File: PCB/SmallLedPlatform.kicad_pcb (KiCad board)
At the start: 4 copper layers, 63.5 x 36.1 mm, 121 parts, among them J101 Conn_01x03_Male, J102 USB_C_Receptacle, J103 Conn_01x03_Male, J104 Conn_02x05_Odd_Even, M101 Fan_4pin, Q101 AO3400A, Q201 IRFR7440TRPBF, Q202 IRFR7440TRPBF, Q301 2N7002, Q302 2N7002, Q303 2N7002, Q304 2N7002, SW401 SW_MEC_5E, SW402 SW_MEC_5E, U101 STM32G0B1CBTx, U102 USBLC6-2P6, U103 TCPP01-M12, U201 LM25118, U202 XC6206PxxxMR, U203 WS3222D, U204 WS3222D, U401 AP3722AT

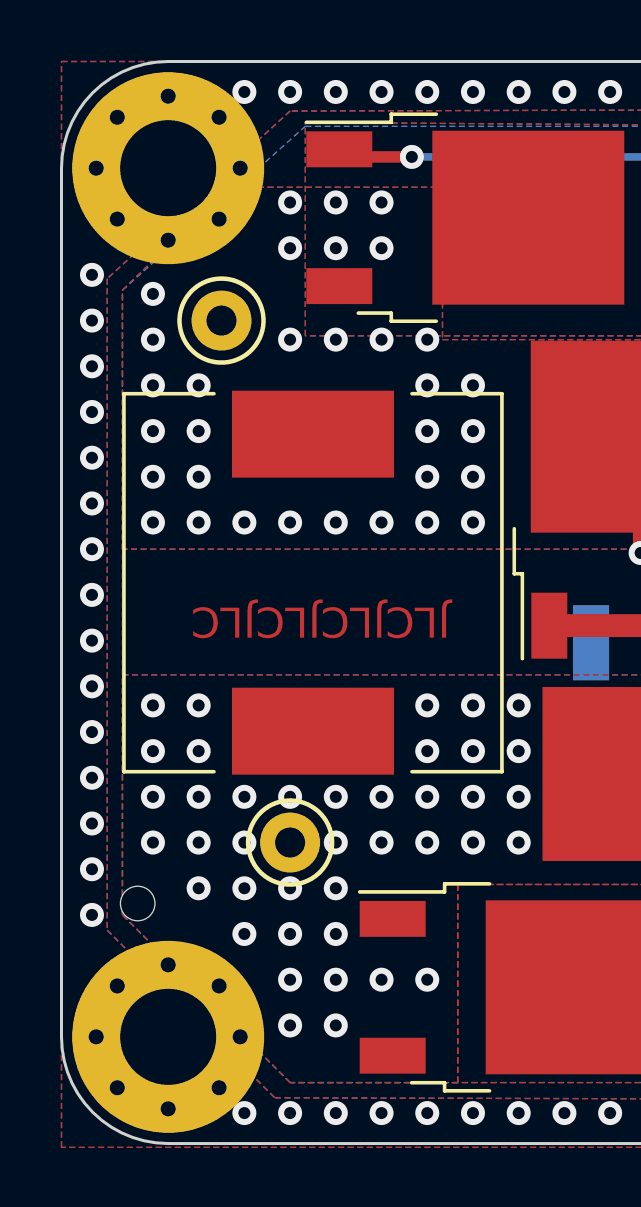
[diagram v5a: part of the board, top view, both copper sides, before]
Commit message: Added hole for fan cable entry
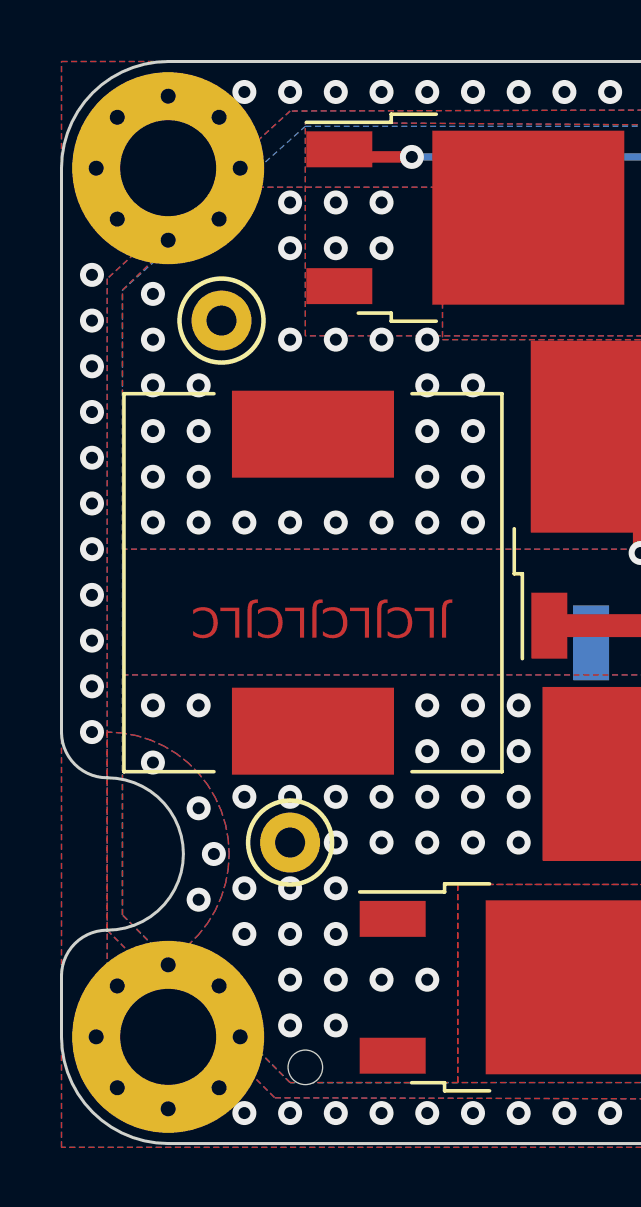
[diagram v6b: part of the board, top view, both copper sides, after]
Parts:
- moved H105 7.81 mm to (99.6, 112.3)
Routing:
- net /Power/dcdc_coil: vias 40 -> 32
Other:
- outline, holes or cut-outs redrawn
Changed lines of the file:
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@@
   )
   (footprint "JLC:JLC_toolinghole" (layer "F.Cu")
-    (at 93.98 106.807)
+    (at 99.568 112.268)
     (property "Sheetfile" "SmallLedPlatform.kicad_sch")
     (property "Sheetname" "")
@@
   (gr_line (start 94.996 78.74) (end 151.384 78.74) (layer "Edge.Cuts") (width 0.1))
   (gr_line (start 154.94 82.296) (end 154.94 111.252) (layer "Edge.Cuts") (width 0.1))
-  (gr_line (start 91.44 111.252) (end 91.44 82.296) (layer "Edge.Cuts") (width 0.1))
+  (gr_line (start 91.44 111.252) (end 91.44 109.22) (layer "Edge.Cuts") (width 0.1))
   (gr_arc (start 151.384 78.74) (mid 153.898472 79.781528) (end 154.94 82.296) (layer "Edge.Cuts") (width 0.1))
   (gr_arc (start 91.44 82.296) (mid 92.481528 79.781528) (end 94.996 78.74) (layer "Edge.Cuts") (width 0.1))
+  (gr_arc (start 91.44 109.22) (mid 91.886369 108.142369) (end 92.964 107.696) (layer "Edge.Cuts") (width 0.1))
+  (gr_arc (start 92.964 102.616) (mid 95.504 105.156) (end 92.964 107.696) (layer "Edge.Cuts") (width 0.1))
+  (gr_arc (start 92.964 102.616) (mid 91.886369 102.169631) (end 91.44 101.092) (layer "Edge.Cuts") (width 0.1))
+  (gr_line (start 91.44 101.092) (end 91.44 82.296) (layer "Edge.Cuts") (width 0.1))
   (gr_arc (start 94.996 114.808) (mid 92.481528 113.766472) (end 91.44 111.252) (layer "Edge.Cuts") (width 0.1))
   (gr_text "JLCJLCJLCJLC" (at 100.076 97.409 180) (layer "F.Cu")
@@
   (via (at 108.204 79.756) (size 0.8) (drill 0.4) (layers "F.Cu" "B.Cu") (free) (net 7))
   (via (at 99.06 79.756) (size 0.8) (drill 0.4) (layers "F.Cu" "B.Cu") (free) (net 7))
+  (via (at 96.012 106.68) (size 0.8) (drill 0.4) (layers "F.Cu" "B.Cu") (free) (net 7))
   (via (at 129.54 113.792) (size 0.8) (drill 0.4) (layers "F.Cu" "B.Cu") (free) (net 7))
   (via (at 126.492 79.756) (size 0.8) (drill 0.4) (layers "F.Cu" "B.Cu") (free) (net 7))
@@
   (via (at 92.456 101.092) (size 0.8) (drill 0.4) (layers "F.Cu" "B.Cu") (free) (net 7))
   (via (at 92.456 93.472) (size 0.8) (drill 0.4) (layers "F.Cu" "B.Cu") (free) (net 7))
+  (via (at 94.488 102.108) (size 0.8) (drill 0.4) (layers "F.Cu" "B.Cu") (free) (net 7))
   (via (at 103.632 113.792) (size 0.8) (drill 0.4) (layers "F.Cu" "B.Cu") (free) (net 7))
   (via (at 105.156 113.792) (size 0.8) (drill 0.4) (layers "F.Cu" "B.Cu") (free) (net 7))
@@
   (via (at 92.456 99.568) (size 0.8) (drill 0.4) (layers "F.Cu" "B.Cu") (free) (net 7))
   (via (at 140.208 113.792) (size 0.8) (drill 0.4) (layers "F.Cu" "B.Cu") (free) (net 7))
-  (via (at 92.456 102.616) (size 0.8) (drill 0.4) (layers "F.Cu" "B.Cu") (free) (net 7))
   (via (at 143.256 113.792) (size 0.8) (drill 0.4) (layers "F.Cu" "B.Cu") (free) (net 7))
   (via (at 132.588 79.756) (size 0.8) (drill 0.4) (layers "F.Cu" "B.Cu") (free) (net 7))
@@
   (via (at 92.456 91.948) (size 0.8) (drill 0.4) (layers "F.Cu" "B.Cu") (free) (net 7))
   (via (at 141.732 113.792) (size 0.8) (drill 0.4) (layers "F.Cu" "B.Cu") (free) (net 7))
+  (via (at 96.012 103.632) (size 0.8) (drill 0.4) (layers "F.Cu" "B.Cu") (free) (net 7))
   (via (at 109.728 113.792) (size 0.8) (drill 0.4) (layers "F.Cu" "B.Cu") (free) (net 7))
   (via (at 100.584 113.792) (size 0.8) (drill 0.4) (layers "F.Cu" "B.Cu") (free) (net 7))
@@
   (via (at 105.156 79.756) (size 0.8) (drill 0.4) (layers "F.Cu" "B.Cu") (free) (net 7))
   (via (at 153.924 88.9) (size 0.8) (drill 0.4) (layers "F.Cu" "B.Cu") (free) (net 7))
-  (via (at 92.456 104.14) (size 0.8) (drill 0.4) (layers "F.Cu" "B.Cu") (free) (net 7))
   (via (at 102.108 113.792) (size 0.8) (drill 0.4) (layers "F.Cu" "B.Cu") (free) (net 7))
   (via (at 117.348 79.756) (size 0.8) (drill 0.4) (layers "F.Cu" "B.Cu") (free) (net 7))
@@
   (via (at 106.68 79.756) (size 0.8) (drill 0.4) (layers "F.Cu" "B.Cu") (free) (net 7))
   (via (at 135.636 113.792) (size 0.8) (drill 0.4) (layers "F.Cu" "B.Cu") (free) (net 7))
-  (via (at 92.456 107.188) (size 0.8) (drill 0.4) (layers "F.Cu" "B.Cu") (free) (net 7))
+  (via (at 96.52 105.156) (size 0.8) (drill 0.4) (layers "F.Cu" "B.Cu") (free) (net 7))
   (via (at 106.68 113.792) (size 0.8) (drill 0.4) (layers "F.Cu" "B.Cu") (free) (net 7))
   (via (at 92.456 87.376) (size 0.8) (drill 0.4) (layers "F.Cu" "B.Cu") (free) (net 7))
@@
   (via (at 111.252 113.792) (size 0.8) (drill 0.4) (layers "F.Cu" "B.Cu") (free) (net 7))
   (via (at 131.064 113.792) (size 0.8) (drill 0.4) (layers "F.Cu" "B.Cu") (free) (net 7))
-  (via (at 92.456 105.664) (size 0.8) (drill 0.4) (layers "F.Cu" "B.Cu") (free) (net 7))
   (via (at 153.924 91.948) (size 0.8) (drill 0.4) (layers "F.Cu" "B.Cu") (free) (net 7))
   (via (at 146.304 79.756) (size 0.8) (drill 0.4) (layers "F.Cu" "B.Cu") (free) (net 7))
@@
   (segment (start 125.592562 95.982) (end 125.592562 96.028633) (width 0.254) (layer "F.Cu") (net 43))
   (segment (start 124.649195 96.972) (end 124.576562 96.972) (width 0.254) (layer "F.Cu") (net 43))
-  (via (at 94.488 104.775) (size 0.8) (drill 0.4) (layers "F.Cu" "B.Cu") (free) (net 44))
   (via (at 102.108 104.775) (size 0.8) (drill 0.4) (layers "F.Cu" "B.Cu") (free) (net 44))
   (via (at 99.06 103.251) (size 0.8) (drill 0.4) (layers "F.Cu" "B.Cu") (free) (net 44))
@@
   (via (at 97.536 106.299) (size 0.8) (drill 0.4) (layers "F.Cu" "B.Cu") (free) (net 44))
   (via (at 99.06 110.871) (size 0.8) (drill 0.4) (layers "F.Cu" "B.Cu") (free) (net 44))
-  (via (at 96.012 101.727) (size 0.8) (drill 0.4) (layers "F.Cu" "B.Cu") (free) (net 44))
   (via (at 103.632 100.203) (size 0.8) (drill 0.4) (layers "F.Cu" "B.Cu") (free) (net 44))
   (via (at 100.584 106.299) (size 0.8) (drill 0.4) (layers "F.Cu" "B.Cu") (free) (net 44))
@@
   (via (at 102.108 109.347) (size 0.8) (drill 0.4) (layers "F.Cu" "B.Cu") (free) (net 44))
   (via (at 103.632 104.775) (size 0.8) (drill 0.4) (layers "F.Cu" "B.Cu") (free) (net 44))
-  (via (at 96.012 103.251) (size 0.8) (drill 0.4) (layers "F.Cu" "B.Cu") (free) (net 44))
   (via (at 100.584 107.823) (size 0.8) (drill 0.4) (layers "F.Cu" "B.Cu") (free) (net 44))
-  (via (at 94.488 103.251) (size 0.8) (drill 0.4) (layers "F.Cu" "B.Cu") (free) (net 44))
-  (via (at 96.012 106.299) (size 0.8) (drill 0.4) (layers "F.Cu" "B.Cu") (free) (net 44))
   (via (at 106.68 100.203) (size 0.8) (drill 0.4) (layers "F.Cu" "B.Cu") (free) (net 44))
-  (via (at 97.536 104.775) (size 0.8) (drill 0.4) (layers "F.Cu" "B.Cu") (free) (net 44))
   (via (at 102.108 103.251) (size 0.8) (drill 0.4) (layers "F.Cu" "B.Cu") (free) (net 44))
   (via (at 100.584 104.775) (size 0.8) (drill 0.4) (layers "F.Cu" "B.Cu") (free) (net 44))
@@
   (via (at 100.584 103.251) (size 0.8) (drill 0.4) (layers "F.Cu" "B.Cu") (free) (net 44))
   (via (at 105.156 101.727) (size 0.8) (drill 0.4) (layers "F.Cu" "B.Cu") (free) (net 44))
-  (via (at 94.488 101.727) (size 0.8) (drill 0.4) (layers "F.Cu" "B.Cu") (free) (net 44))
   (via (at 106.68 103.251) (size 0.8) (drill 0.4) (layers "F.Cu" "B.Cu") (free) (net 44))
   (via (at 99.06 107.823) (size 0.8) (drill 0.4) (layers "F.Cu" "B.Cu") (free) (net 44))
   (via (at 103.632 103.251) (size 0.8) (drill 0.4) (layers "F.Cu" "B.Cu") (free) (net 44))
   (via (at 99.06 109.347) (size 0.8) (drill 0.4) (layers "F.Cu" "B.Cu") (free) (net 44))
-  (via (at 96.012 104.775) (size 0.8) (drill 0.4) (layers "F.Cu" "B.Cu") (free) (net 44))
   (via (at 96.012 100.203) (size 0.8) (drill 0.4) (layers "F.Cu" "B.Cu") (free) (net 44))
   (via (at 100.584 110.871) (size 0.8) (drill 0.4) (layers "F.Cu" "B.Cu") (free) (net 44))
@@
     )
   )
+  (zone (net 7) (net_name "SHIELD") (layers "F.Cu" "In1.Cu" "In2.Cu" "B.Cu") (hatch edge 0.508)
+    (priority 1001)
+    (connect_pads no (clearance 0.254))
+    (min_thickness 0.1) (filled_areas_thickness no)
+    (fill yes (thermal_gap 0.508) (thermal_bridge_width 0.508) (island_removal_mode 1) (island_area_min 0))
+    (polygon
+      (pts
+        (arc (start 92.964 109.22) (mid 97.028 105.156) (end 92.964 101.092))
+      )
+    )
+  )
   (zone (net 5) (net_name "IN") (layer "F.Cu") (hatch edge 0.508)
     (priority 1)
@@
       )
     )
+  )
+  (zone (net 0) (net_name "") (layers *.Mask) (hatch edge 0.508)
+    (priority 1001)
+    (connect_pads no (clearance 0.254))
+    (min_thickness 0.254) (filled_areas_thickness no)
+    (fill yes (thermal_gap 0.508) (thermal_bridge_width 0.508))
+    (polygon
+      (pts
+        (arc (start 92.964 109.22) (mid 97.028 105.156) (end 92.964 101.092))
+      )
+    )

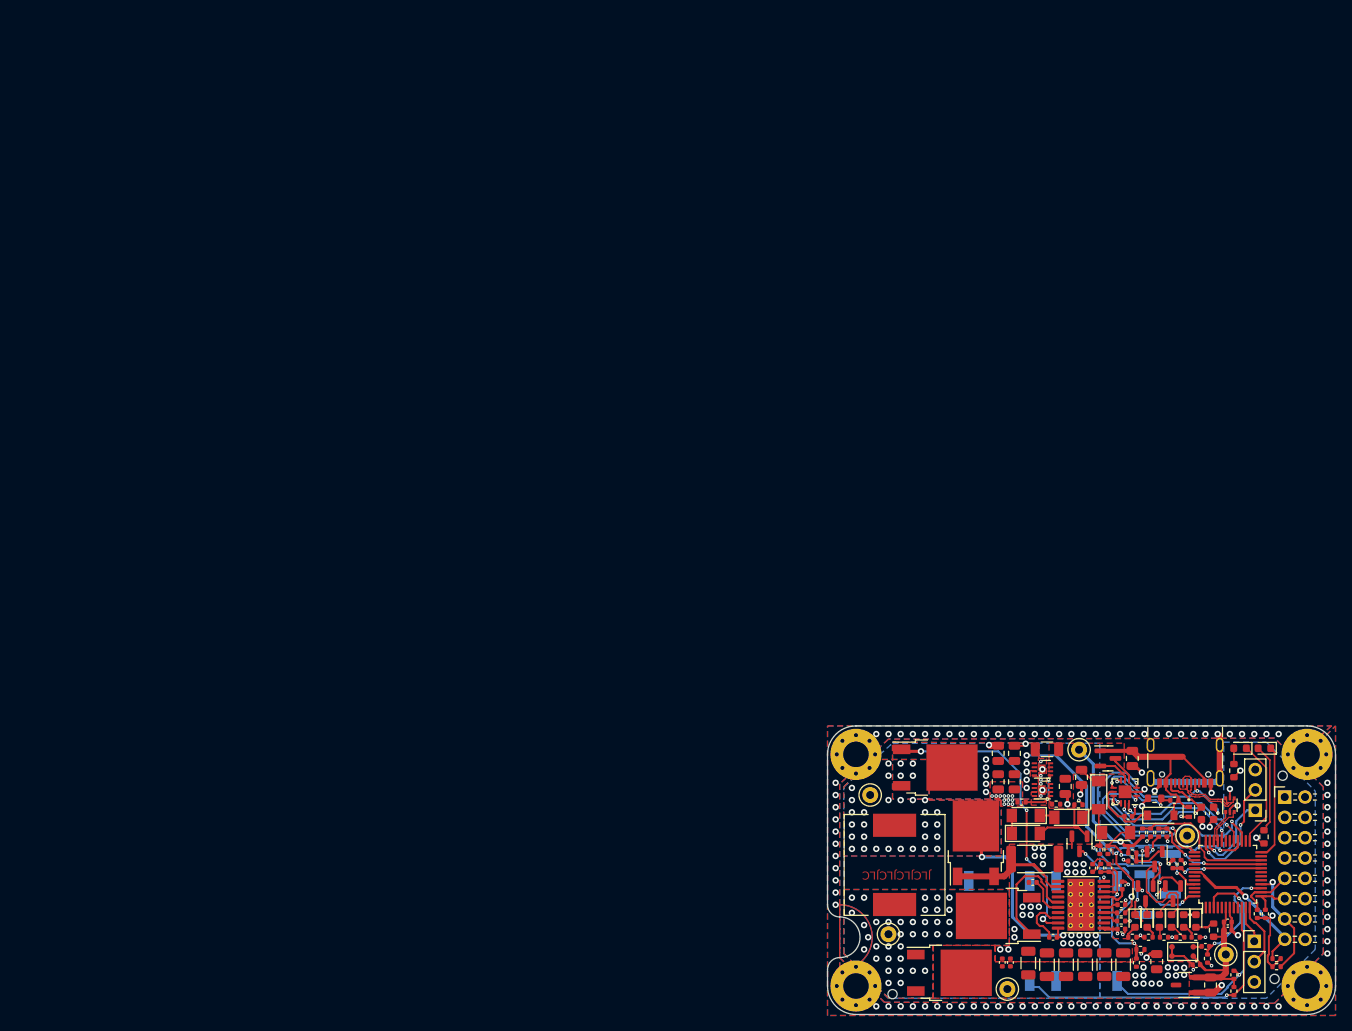
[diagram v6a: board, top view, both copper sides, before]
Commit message: Fix DRC and outline
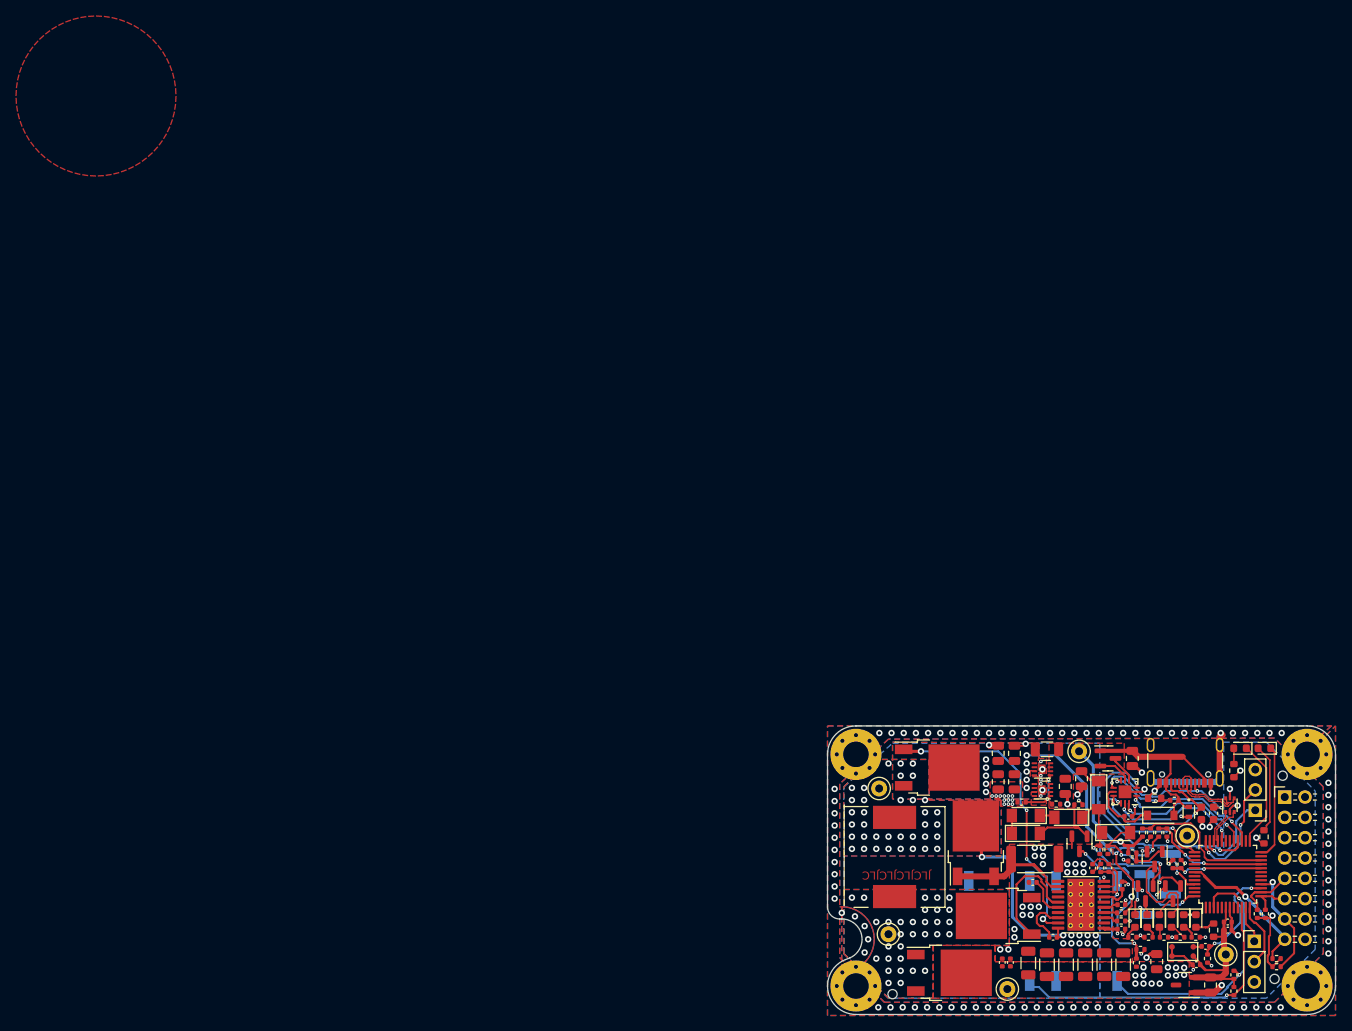
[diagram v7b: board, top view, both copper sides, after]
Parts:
- moved TP202 1.38 mm to (97.9, 86.6)
- moved L201 0.99 mm to (99.8, 95.1)
- moved Q201 0.25 mm to (105.2, 83.9)
- moved TP103 0.20 mm to (122.9, 81.9)
- moved C103 0.18 mm to (123.2, 85.3)
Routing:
- net /CC2_MCU: track 29.5 -> 17.9 mm
- net /Power/Power LEDS/20v_led_k: track 14.4 -> 13.3 mm
- net /VBUS_CTRL: track 9.38 -> 8.49 mm
- net GND: track 47.2 -> 47.1 mm, vias 82 -> 81
- net /Power/dcdc_coil: vias 32 -> 31
- net /Power/HS: vias 34 -> 38
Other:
- outline, holes or cut-outs redrawn

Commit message: Add production text to PCB
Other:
- board text added: "2023-02-11"
- board text added: "Rev1"
- board text added: "Skrooter Audio"
- board text added: "Small Led Platform"
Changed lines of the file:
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@@
     (effects (font (size 1 1.016) (thickness 0.1524)))
+  )
+  (gr_text "Small Led Platform" (at 116.2304 92.1766) (layer "B.SilkS")
+    (effects (font (size 1.016 1.016) (thickness 0.127)) (justify mirror))
+  )
+  (gr_text "2023-02-11" (at 111.252 93.98) (layer "B.SilkS")
+    (effects (font (size 1 1) (thickness 0.15)) (justify mirror))
+  )
+  (gr_text "Rev1" (at 121.92 93.98) (layer "B.SilkS")
+    (effects (font (size 1 1) (thickness 0.15)) (justify mirror))
+  )
+  (gr_text "Skrooter Audio" (at 115.316 90.424) (layer "B.SilkS")
+    (effects (font (size 1.5 1.5) (thickness 0.254)) (justify mirror))
   )
   (segment (start 136.6012 88.8592) (end 136.1306 88.8592) (width 0.25) (layer "F.Cu") (net 1))
